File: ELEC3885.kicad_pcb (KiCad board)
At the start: 4 copper layers, 190 x 145.2 mm, 152 parts, among them J1 MicInstIn, J2 LineIn, J3 HeadPhoneOut, J4 Conn_01x05_Female, J5 LineOutR, J6 LineOutL, J7 USB_B_Micro, J8 Conn_LiPo, SW1 SW_SPST, SW10 RotaryEncoder_Switch, SW11 RotaryEncoder_Switch, SW12 RotaryEncoder_Switch, SW13 RotaryEncoder_Switch, SW14 SW_Push, SW15 SW_Push, SW16 SW_Push, SW17 SW_Push, SW2 SW_Push, SW3 SW_Push, SW4 SW_Push, SW5 SW_Push, SW6 SW_Push, SW7 SW_Push, SW8 SW_Push, SW9 SW_Push, U1 NE5532, U10 74HC595, U11 LCD_Conn, U2 AP7313, U3 SGTL5000XNLA3, U4 Teensy4.1, U5 MCP73831-2-OT, U6 MT3608, U7 L7805, U8 74HC595, U9 74HC595

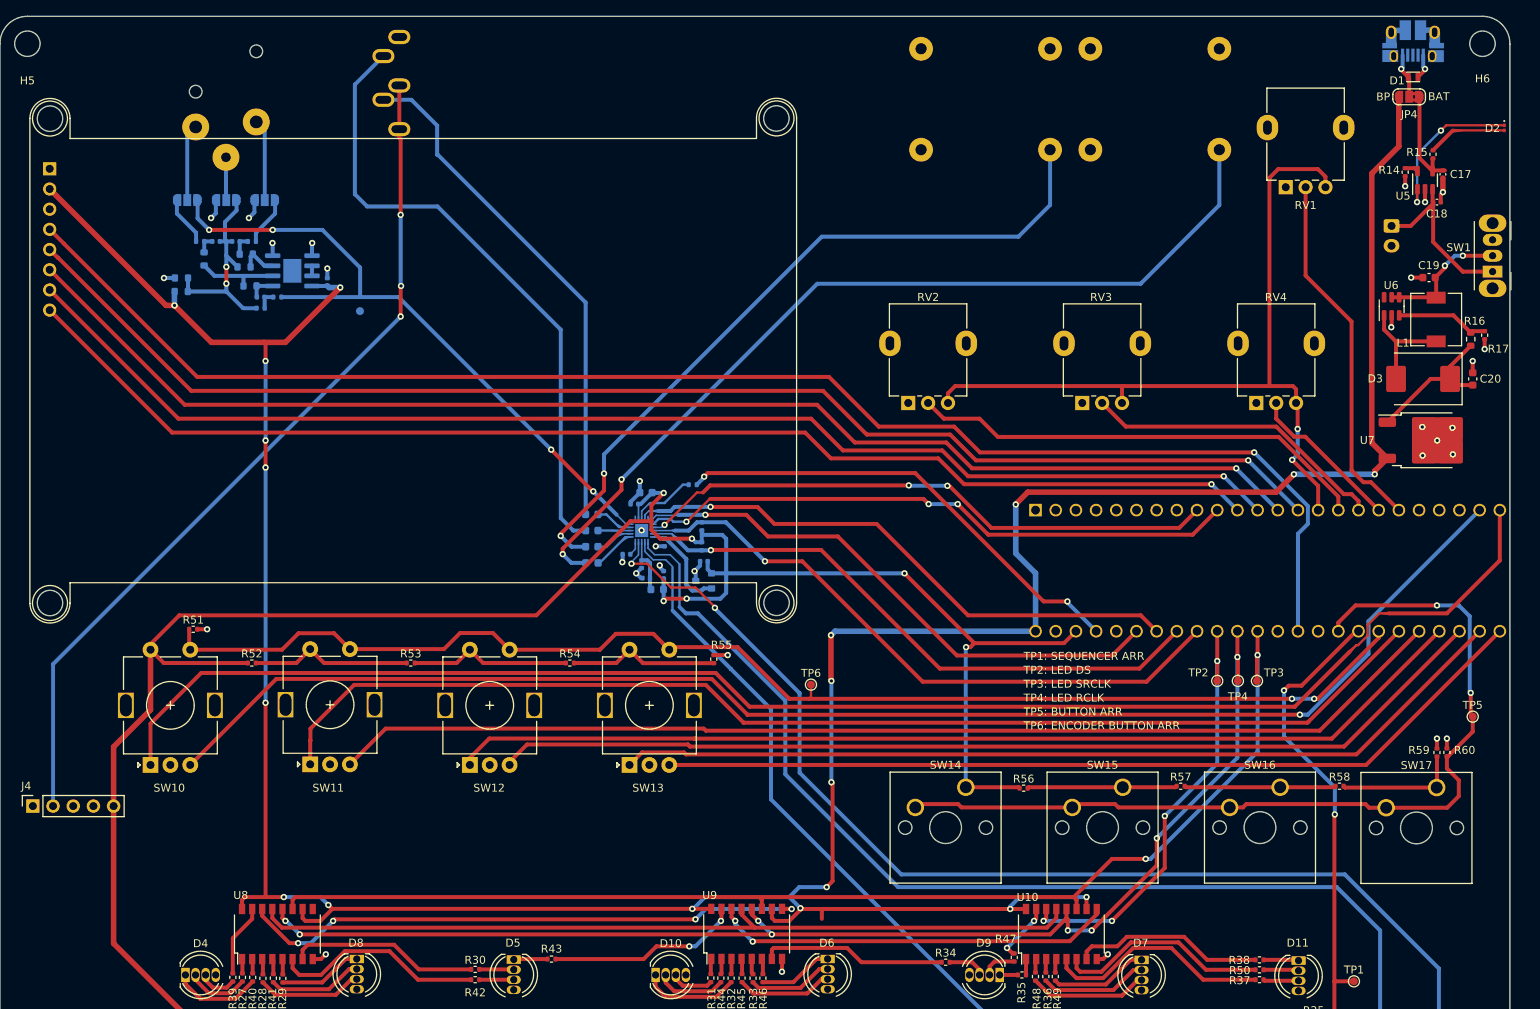
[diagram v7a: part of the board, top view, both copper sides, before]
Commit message: LED foorprint fix, ground planes fix
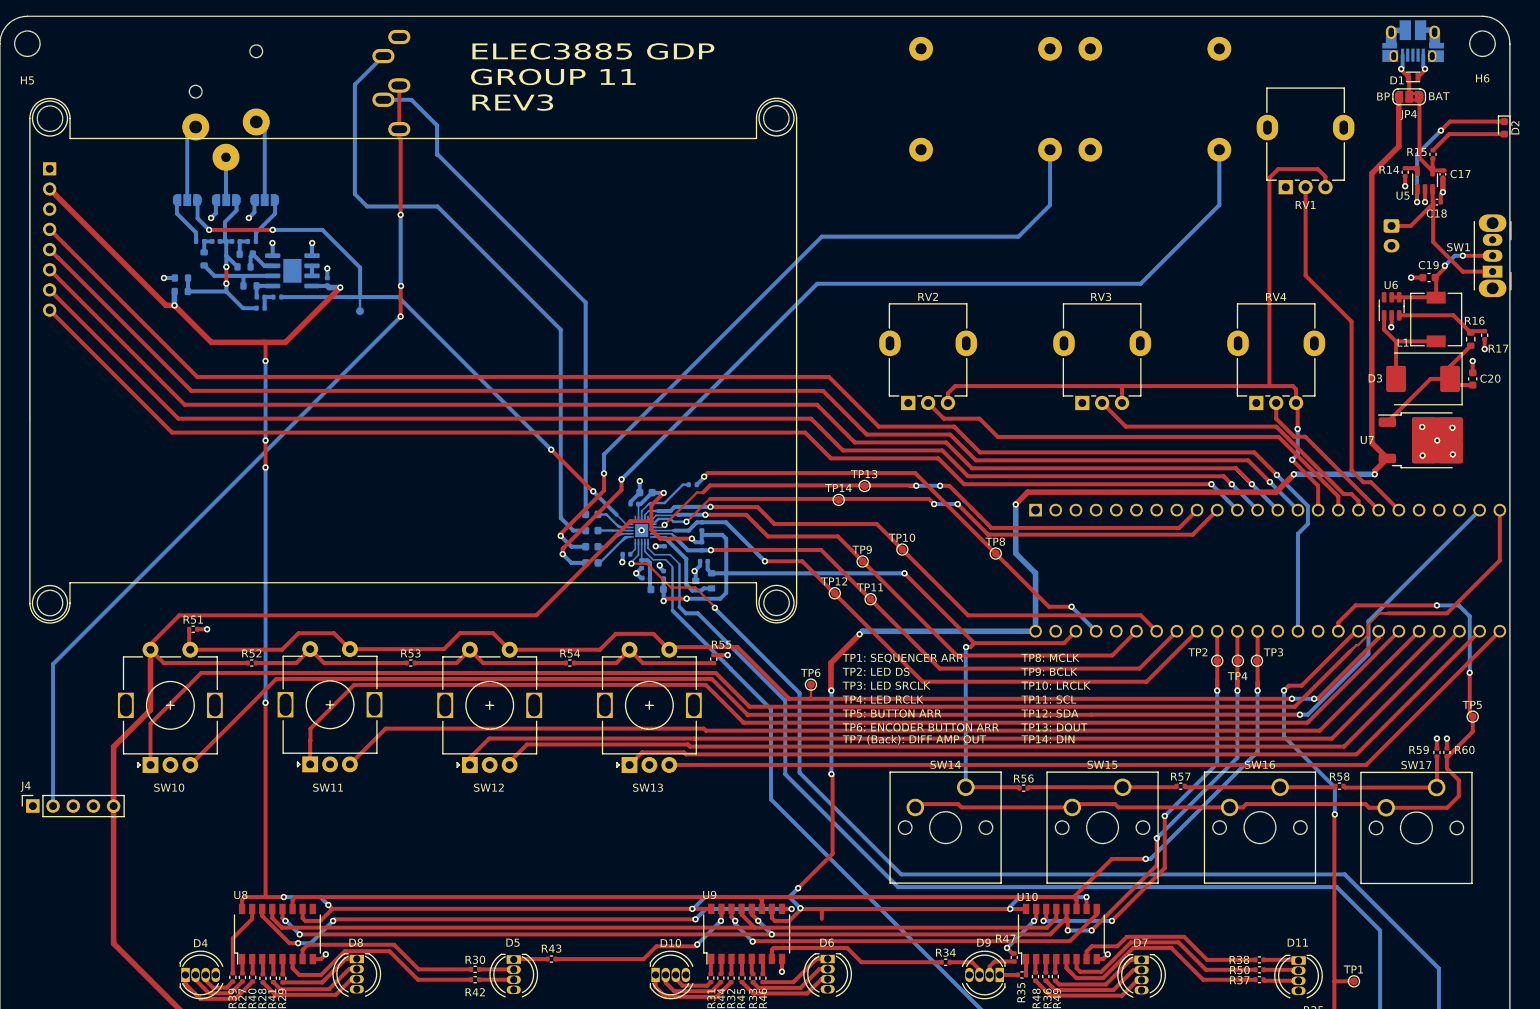
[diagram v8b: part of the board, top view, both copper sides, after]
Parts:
- added TP10: TP_LRCLK, TestPoint:TestPoint_Pad_D1.0mm, F.Cu at (133.8, 83.8)
- added TP11: TP_SCL, TestPoint:TestPoint_Pad_D1.0mm, F.Cu at (129.8, 90.0)
- added TP12: TP_SDA, TestPoint:TestPoint_Pad_D1.0mm, F.Cu at (125.2, 89.2)
- added TP13: TP_DOUT, TestPoint:TestPoint_Pad_D1.0mm, F.Cu at (129.0, 75.8)
- added TP14: TP_DIN, TestPoint:TestPoint_Pad_D1.0mm, F.Cu at (125.8, 77.5)
- added TP8: TP_MCLK, TestPoint:TestPoint_Pad_D1.0mm, F.Cu at (145.5, 84.2)
- added TP9: TP_BCLK, TestPoint:TestPoint_Pad_D1.0mm, F.Cu at (128.8, 85.2)
- D2: footprint LED_SMD:LED_0201_0603Metric -> LED_SMD:LED_0603_1608Metric
- moved TP2 2.53 mm to (173.4, 97.8)
- moved TP3 2.53 mm to (178.4, 97.8)
- moved TP4 2.53 mm to (176.0, 97.8)
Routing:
- net +5V: track 428.8 -> 424.7 mm
- net /Teensy/LCD_MOSI: track 167.0 -> 169.8 mm
- net /Teensy/LED_SRCLK: track 152.0 -> 149.9 mm
- net /Teensy/LED_RCLK: track 159.8 -> 158.0 mm
- net /Audio/MIC_IN: track 84.7 -> 86.5 mm
- net /Teensy/LED_DS: track 54.7 -> 53.4 mm
- net Net-(D2-K): track 20.0 -> 21.2 mm
- net /Audio/D_OUT: track 73.3 -> 74.3 mm
- added copper zone on In2.Cu, net GND
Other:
- board text added: "ELEC3885 GDP GROUP 11 REV3"
- board text added: "TP10: LRCLK"
- board text added: "TP11: SCL"
- board text added: "TP12: SDA"
- board text added: "TP13: DOUT"
- board text added: "TP14: DIN"
- board text added: "TP7 (Back): DIFF AMP OUT"
- board text added: "TP8: MCLK"
- board text added: "TP9: BCLK"
- board text removed: "TP7: DIFF AMP OUT"
